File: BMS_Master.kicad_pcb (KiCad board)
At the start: 2 copper layers, 65 x 45 mm, 82 parts, among them J1 PWR, J2 PROG, J3 BMS_M_OUT, J4 BMS_M_IN, J5 CAN, Q1 BC807, SW1 SW_SPST, U1 AP2204K-ADJ, U2 AP2204K-ADJ, U3 STM32F103C8Tx, U4 BQ79600-Q1, U5 SN65HVD256D, Y1 8M, Y2 32.768k

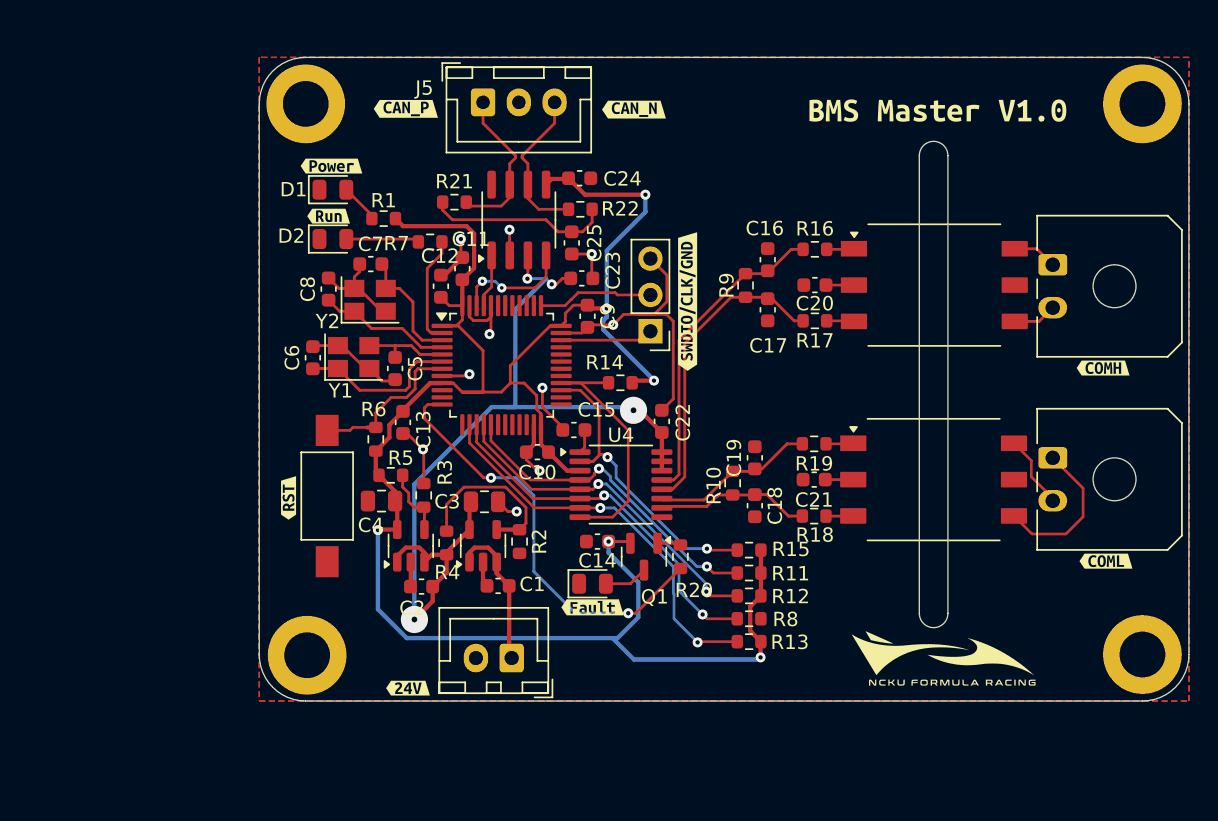
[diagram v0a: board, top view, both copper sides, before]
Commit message: Add via holes and teardrops
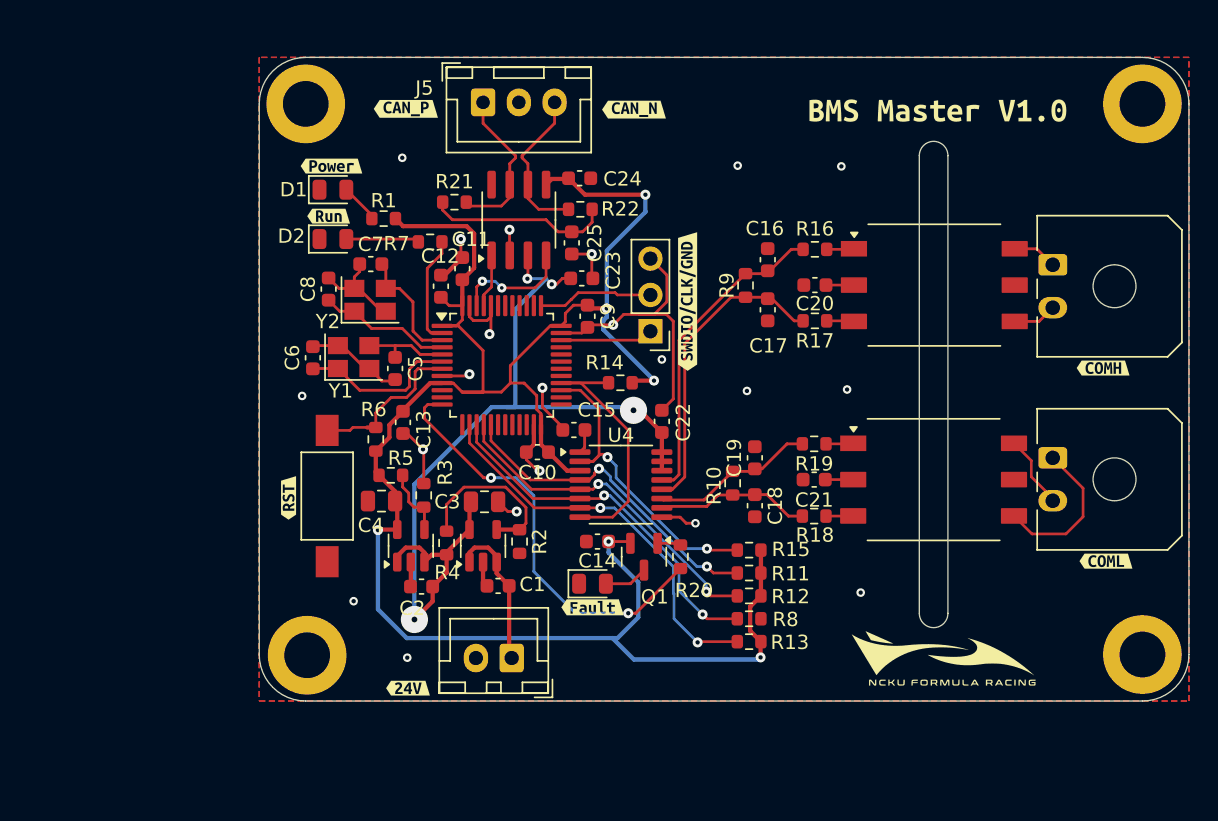
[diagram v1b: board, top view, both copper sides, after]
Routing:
- net GND: track 66.9 -> 69.4 mm, vias 10 -> 21

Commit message: Fix layout problems
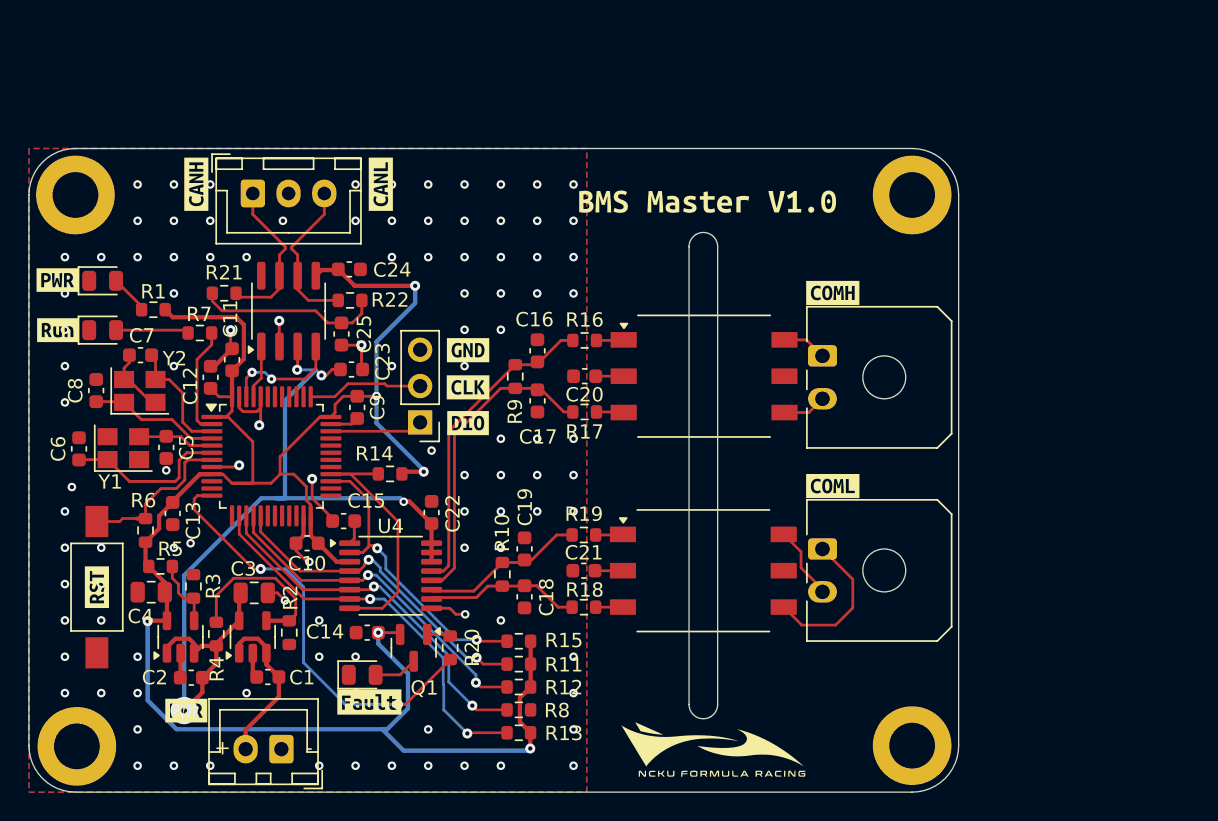
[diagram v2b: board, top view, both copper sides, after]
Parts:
- removed kibuzzard-6797B0CB: G***, kibuzzard-6797B0CB
- removed kibuzzard-6797B107: G***, kibuzzard-6797B107
- removed kibuzzard-6797B129: G***, kibuzzard-6797B129
- removed kibuzzard-6797B18E: G***, kibuzzard-6797B18E
- removed kibuzzard-6797B1AA: G***, kibuzzard-6797B1AA
- removed kibuzzard-6797B21F: G***, kibuzzard-6797B21F
- removed kibuzzard-6797B237: G***, kibuzzard-6797B237
- removed kibuzzard-6797BA30: G***, kibuzzard-6797BA30
- removed kibuzzard-6797BA57: G***, kibuzzard-6797BA57
- removed kibuzzard-6797BA64: G***, kibuzzard-6797BA64
- added kibuzzard-679F52AD: G***, kibuzzard-679F52AD, F.Cu at (54.1, 56.1)
- added kibuzzard-679F52BD: G***, kibuzzard-679F52BD, F.Cu at (54.1, 52.6)
- added kibuzzard-679F550D: G***, kibuzzard-679F550D, F.Cu at (108.3, 53.5)
- added kibuzzard-679F551A: G***, kibuzzard-679F551A, F.Cu at (108.3, 67.0)
- added kibuzzard-679F5580: G***, kibuzzard-679F5580, F.Cu at (56.9, 74.1)
- added kibuzzard-679F55A0: G***, kibuzzard-679F55A0, F.Cu at (76.7, 45.9)
- added kibuzzard-679F55DD: G***, kibuzzard-679F55DD, F.Cu at (63.8, 45.9)
- added kibuzzard-679F55F7: G***, kibuzzard-679F55F7, F.Cu at (75.9, 82.1)
- added kibuzzard-679F561D: G***, kibuzzard-679F561D, F.Cu at (63.1, 82.7)
- added kibuzzard-679F5696: G***, kibuzzard-679F5696, F.Cu at (82.8, 57.5)
- added kibuzzard-679F56A0: G***, kibuzzard-679F56A0, F.Cu at (82.8, 60.1)
- added kibuzzard-679F56A8: G***, kibuzzard-679F56A8, F.Cu at (82.8, 62.6)
- moved C8 17.7 mm to (56.8, 60.3)
- moved C6 17.5 mm to (55.6, 64.4)
- moved C10 17.3 mm to (71.5, 71.0)
- moved C11 17.3 mm to (66.3, 58.2)
- moved C15 17.3 mm to (74.1, 69.5)
- moved C3 17.3 mm to (67.8, 74.5)
- moved J4 17.3 mm to (107.6, 71.4)
- moved R1 17.3 mm to (60.8, 54.7)
- moved R11 17.3 mm to (86.3, 79.5)
- moved R13 17.3 mm to (86.3, 84.2)
- moved R14 17.3 mm to (77.3, 66.2)
- moved R2 17.3 mm to (70.3, 77.2)
- moved R20 17.3 mm to (81.5, 78.3)
- moved R22 17.3 mm to (74.5, 54.0)
- moved R5 17.3 mm to (61.3, 72.6)
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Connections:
- H1 pad 1: GND -> unconnected-(H1-Pad1)
- H2 pad 1: GND -> unconnected-(H2-Pad1)
- H3 pad 1: GND -> unconnected-(H3-Pad1)
- H4 pad 1: GND -> unconnected-(H4-Pad1)
- J1 pad 1: +24V -> GND
- J1 pad 2: GND -> +24V
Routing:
- net GND: track 69.4 -> 37.1 mm, vias 21 -> 104
- net Net-(U3-PD0): track 6.27 -> 5.34 mm
- net +24V: track 10.5 -> 11.4 mm
- net (no net): vias 0 -> 3
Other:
- rule pad_to_mask_clearance: 0.08 -> 0
- board text added: "+ -"

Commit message: Add size label in user layer and adjust sheet size
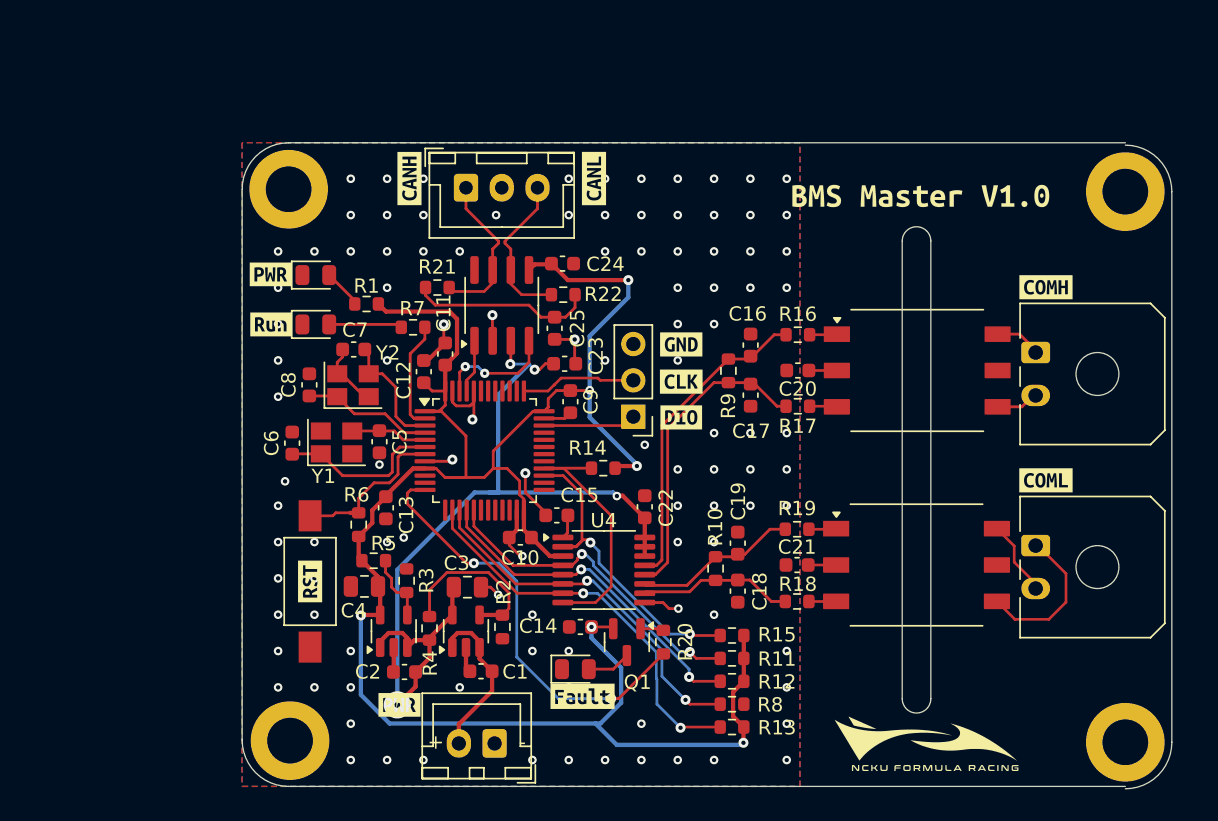
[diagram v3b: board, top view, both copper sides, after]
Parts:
- moved C13 14.9 mm to (77.1, 68.5)
- moved C4 14.9 mm to (75.6, 74.0)
- moved C7 14.9 mm to (74.8, 57.5)
- moved C1 14.9 mm to (83.7, 80.0)
- moved C10 14.9 mm to (86.5, 70.6)
- moved C11 14.9 mm to (81.2, 57.8)
- moved C12 14.9 mm to (79.7, 59.0)
- moved C14 14.9 mm to (90.7, 76.8)
- moved C15 14.9 mm to (89.0, 69.0)
- moved C16 14.9 mm to (102.6, 57.1)
- moved C17 14.9 mm to (102.6, 60.6)
- moved C18 14.9 mm to (101.7, 74.3)
- moved C19 14.9 mm to (101.7, 71.0)
- moved C2 14.9 mm to (78.4, 80.0)
- moved C20 14.9 mm to (105.9, 58.9)
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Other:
- board size 65 x 45 mm -> 65 x 45.2 mm

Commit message: Fix edge cuts and DRC
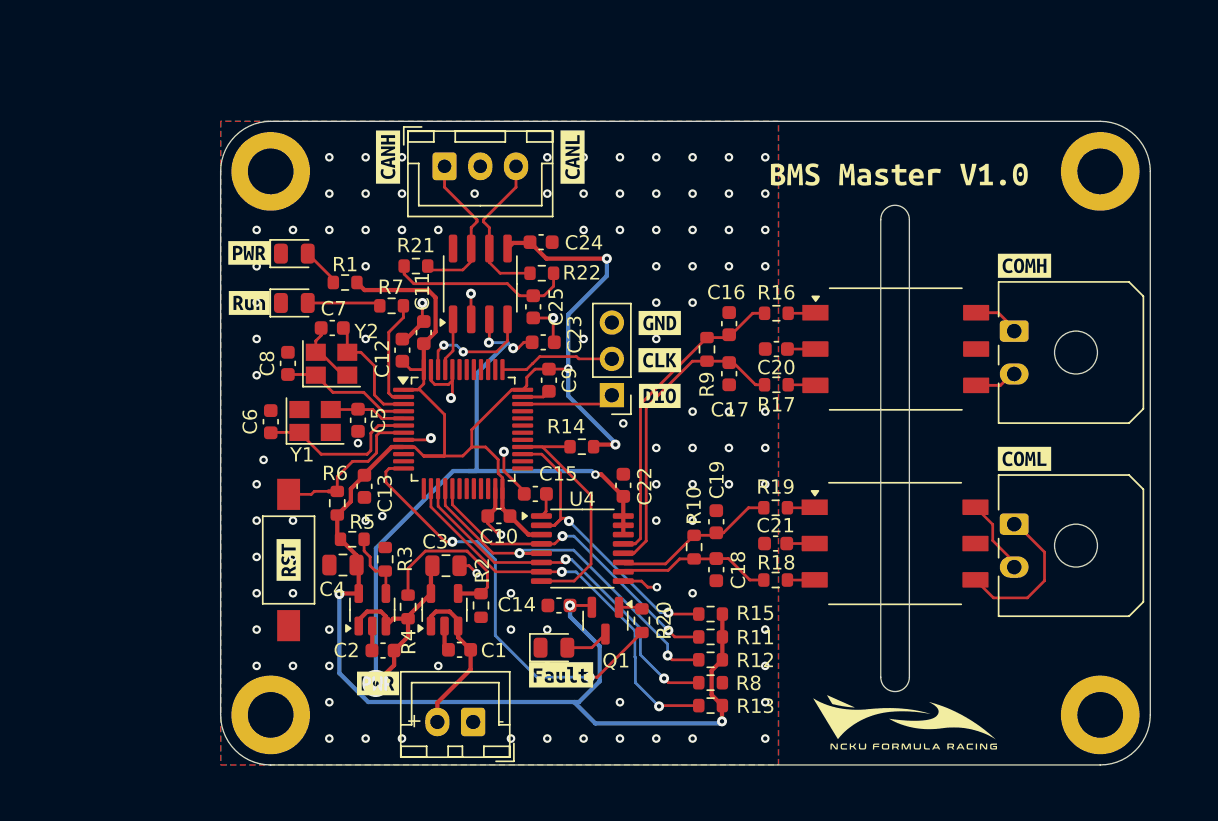
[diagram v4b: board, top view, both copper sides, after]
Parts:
- moved H3 2.60 mm to (127.0, 83.0)
- moved H4 2.25 mm to (127.0, 45.0)
- moved H2 2.25 mm to (69.0, 83.0)
- moved C1 2.12 mm to (82.2, 78.5)
- moved C10 2.12 mm to (85.0, 69.1)
- moved C11 2.12 mm to (79.7, 56.3)
- moved C12 2.12 mm to (78.2, 57.5)
- moved C13 2.12 mm to (75.6, 67.0)
- moved C14 2.12 mm to (89.2, 75.3)
- moved C15 2.12 mm to (87.5, 67.5)
- moved C16 2.12 mm to (101.1, 55.6)
- moved C17 2.12 mm to (101.1, 59.1)
- moved C18 2.12 mm to (100.2, 72.8)
- moved C19 2.12 mm to (100.2, 69.5)
- moved C2 2.12 mm to (76.9, 78.5)
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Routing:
- net MISO: track 24.0 -> 27.1 mm
- net GND: vias 104 -> 105
- net (no net): vias 3 -> 2
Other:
- board size 65 x 45.2 mm -> 65 x 45 mm
- board text added: "R=3.5"
